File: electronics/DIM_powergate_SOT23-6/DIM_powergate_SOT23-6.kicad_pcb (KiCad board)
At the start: 2 copper layers, 13.7 x 11.2 mm, 10 parts, among them J1 Conn_01x04, J2 Conn_01x04, Q1 PMOS, Q2 NMOS

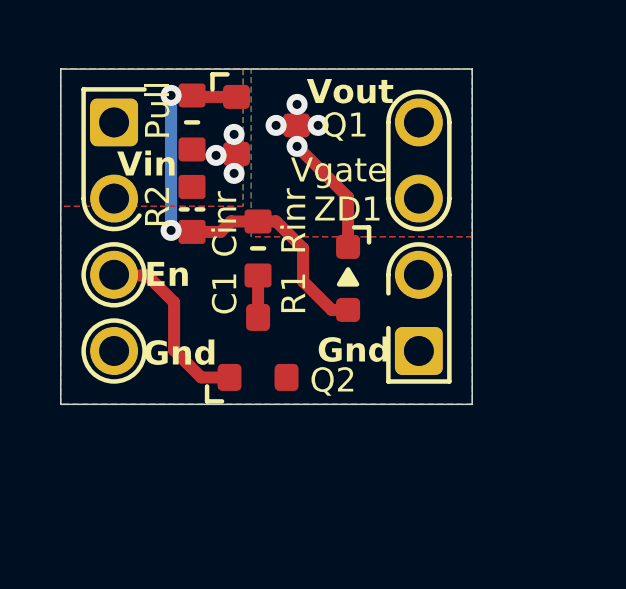
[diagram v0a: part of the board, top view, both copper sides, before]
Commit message: updated SOT23 power gate, added SOT23-6 power gate module
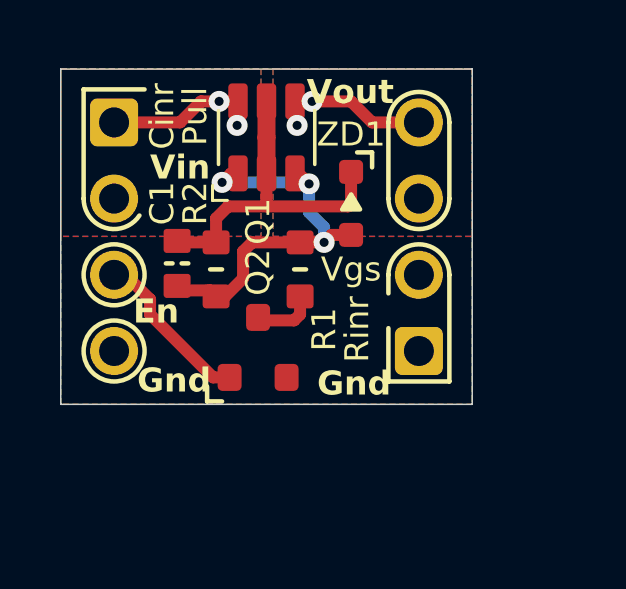
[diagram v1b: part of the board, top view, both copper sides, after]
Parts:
- Q1: value PMOS -> Dual_PMOS; footprint SquantorIC:SOT23-3 -> SquantorIC:SOT23-6-HAND
- ZD1: value Vgate -> Vgs
- moved R2 4.96 mm to (130.4, 43.0), turned to -90 degrees
- moved ZD1 2.50 mm to (134.9, 40.8)
- moved C1 1.87 mm to (129.1, 42.8)
- moved R1 1.57 mm to (133.2, 43.0)
- moved Q1 0.40 mm to (132.1, 38.6), turned to 90 degrees
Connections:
- C1 pad 1: /VIN -> Net-(Q1-S1)
- C1 pad 2: Net-(Q1-G) -> Net-(Q1-G1)
- Q1 pad 1: Net-(Q1-G) -> Net-(Q1-G1)
- Q1 pad 2: /VIN -> Net-(Q1-S1)
- Q1 pad 3: /VOUT -> Net-(Q1-G1)
- R1 pad 1: Net-(Q1-G) -> Net-(Q1-G1)
- R2 pad 1: /VIN -> Net-(Q1-S1)
- R2 pad 2: Net-(Q1-G) -> Net-(Q1-G1)
- ZD1 pad 1: /VOUT -> Net-(Q1-S1)
- ZD1 pad 2: Net-(Q1-G) -> Net-(Q1-G1)
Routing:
- net Net-(Q1-G): track 14.6 -> 0.00 mm, vias 2 -> 0
- net Net-(Q1-G1): track 0.00 -> 13.7 mm, vias 0 -> 3
- net Net-(Q1-S1): track 0.00 -> 11.4 mm
- net /VIN: track 0.00 -> 4.42 mm, vias 3 -> 2
- net Net-(Q2-D): track 1.40 -> 2.12 mm
- net /EN: track 6.18 -> 5.53 mm
- net /VOUT: track 4.05 -> 4.42 mm, vias 4 -> 2

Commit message: Reviewed and fixed
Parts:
- N1: value 20260103 -> 20260110; moved to B.Cu
- N2: moved to B.Cu
- moved N1 47.4 mm to (132.1, 44.3), turned to 180 degrees
- moved N2 47.4 mm to (132.1, 40.6), turned to 180 degrees

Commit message: preparation for production V20260118
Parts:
- N1: value 20260110 -> 20260118
- moved J1 106.5 mm to (21.8, 25.6)
- moved N1 106.5 mm to (26.9, 28.0)
- moved N2 106.5 mm to (26.9, 24.3)
- moved Q1 106.5 mm to (26.9, 22.3)
- moved Q2 106.5 mm to (26.6, 29.3)
- moved R2 106.5 mm to (25.2, 26.7)
- moved ZD1 106.5 mm to (29.7, 24.5)
- moved C1 106.5 mm to (23.9, 26.5)
- moved J2 106.5 mm to (31.9, 25.6)
- moved R1 106.5 mm to (28.0, 26.7)
